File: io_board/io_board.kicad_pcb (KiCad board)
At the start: 2 copper layers, 70 x 100 mm, 54 parts, among them J1 RATE_CV1, J10 CLK_2, J11 SAW_2, J12 MIX, J13 IN2, J14 OUT2, J16 Conn_01x10_Male, J2 PWM_1, J3 CLK_1, J4 SAW_1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

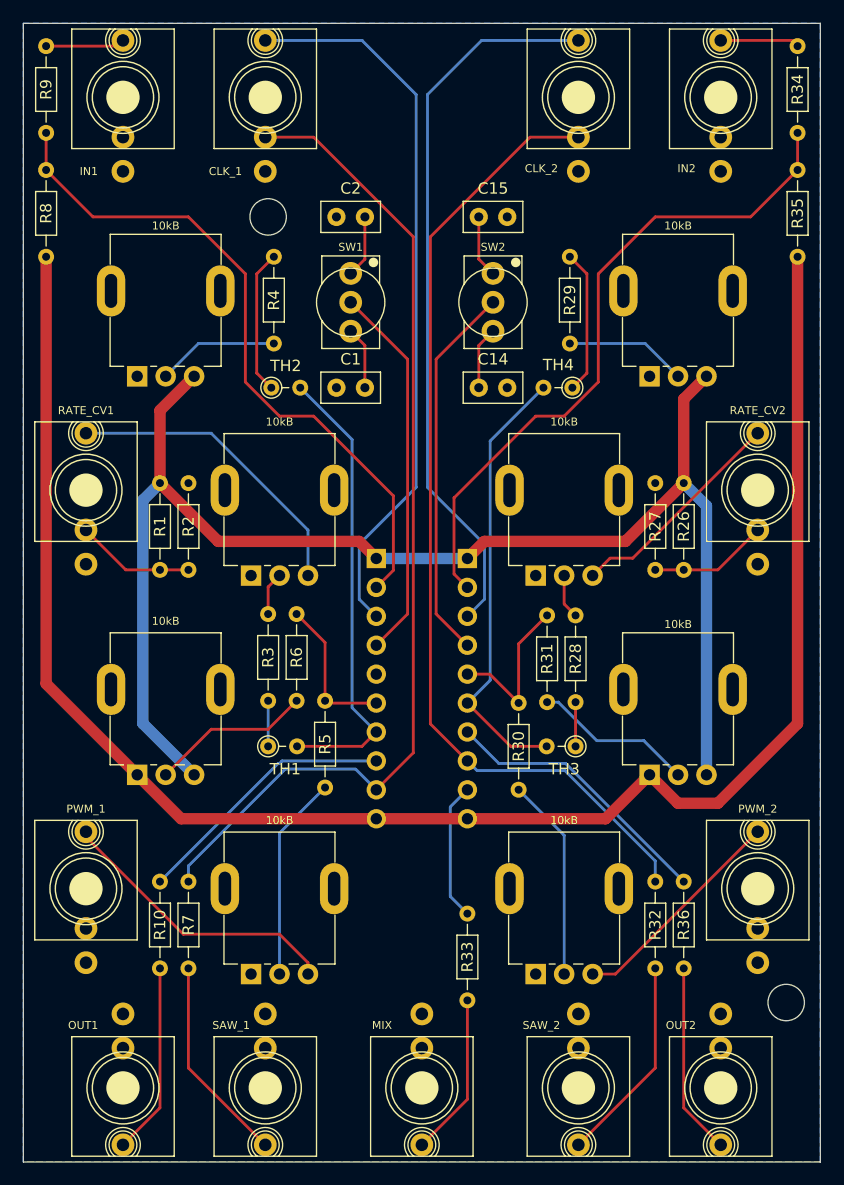
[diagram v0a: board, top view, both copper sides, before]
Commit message: Changed mounting holes
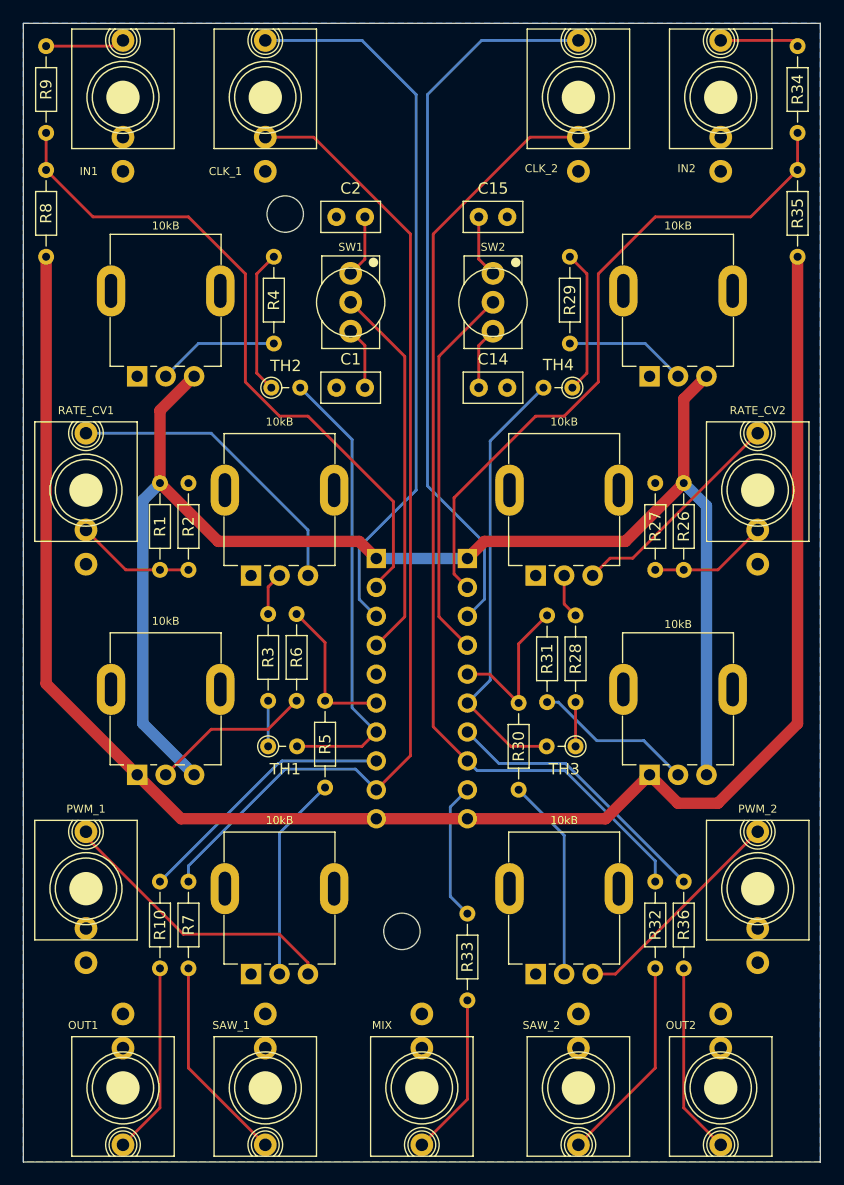
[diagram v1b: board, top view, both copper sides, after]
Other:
- outline, holes or cut-outs redrawn
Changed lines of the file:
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@@
     )
   )
+  (gr_circle (center 23 16.75) (end 24.6 16.75) (layer "Edge.Cuts") (width 0.1) (fill none))
   (gr_rect (start 0 100) (end 70 0) (layer "Edge.Cuts") (width 0.1) (fill none))
-  (gr_circle (center 67 86) (end 68.6 86) (layer "Edge.Cuts") (width 0.1) (fill none))
-  (gr_circle (center 21.5 17) (end 23.1 17) (layer "Edge.Cuts") (width 0.1) (fill none))
+  (gr_circle (center 33.25 79.75) (end 34.85 79.75) (layer "Edge.Cuts") (width 0.1) (fill none))
   (gr_circle (center 57.5 23.5) (end 61.1 23.5) (layer "User.2") (width 0.15) (fill none))
   (gr_circle (center 12.5 58.5) (end 16.1 58.5) (layer "User.2") (width 0.15) (fill none))
@@
   (gr_circle (center 48.75 93.5) (end 51.95 93.5) (layer "User.2") (width 0.15) (fill none))
   (gr_circle (center 22.5 41) (end 26.1 41) (layer "User.2") (width 0.15) (fill none))
-  (gr_line (start 70 50) (end 0 50) (layer "User.2") (width 0.15))
+  (gr_line (start 70.5 50) (end 0.5 50) (layer "User.2") (width 0.15))
   (gr_circle (center 5.5 41) (end 8.7 41) (layer "User.2") (width 0.15) (fill none))
   (gr_circle (center 35 93.5) (end 38.2 93.5) (layer "User.2") (width 0.15) (fill none))
@@
   (segment (start 5.5 71) (end 5.5 71.45) (width 0.25) (layer "F.Cu") (net 8))
   (segment (start 5.5 71.45) (end 14.05 80) (width 0.25) (layer "F.Cu") (net 8))
+  (segment (start 31 52.08) (end 29.5 50.58) (width 0.25) (layer "B.Cu") (net 9))
+  (segment (start 34.5 41) (end 34.5 6.25) (width 0.25) (layer "B.Cu") (net 9))
+  (segment (start 29.5 50.58) (end 29.5 46) (width 0.25) (layer "B.Cu") (net 9))
+  (segment (start 29.5 46) (end 34.5 41) (width 0.25) (layer "B.Cu") (net 9))
+  (segment (start 34.5 6.25) (end 29.75 1.5) (width 0.25) (layer "B.Cu") (net 9))
   (segment (start 29.75 1.5) (end 21.25 1.5) (width 0.25) (layer "B.Cu") (net 9))
-  (segment (start 34.5 6.25) (end 29.75 1.5) (width 0.25) (layer "B.Cu") (net 9))
-  (segment (start 29.5 50.58) (end 29.5 45.75) (width 0.25) (layer "B.Cu") (net 9))
-  (segment (start 29.5 45.75) (end 34.5 40.75) (width 0.25) (layer "B.Cu") (net 9))
-  (segment (start 31 52.08) (end 29.5 50.58) (width 0.25) (layer "B.Cu") (net 9))
-  (segment (start 34.5 40.75) (end 34.5 6.25) (width 0.25) (layer "B.Cu") (net 9))
-  (segment (start 34.25 18.75) (end 25.5 10) (width 0.25) (layer "F.Cu") (net 10))
+  (segment (start 34 64.32) (end 34 18.5) (width 0.25) (layer "F.Cu") (net 10))
   (segment (start 25.5 10) (end 21.25 10) (width 0.25) (layer "F.Cu") (net 10))
-  (segment (start 31 67.32) (end 34.25 64.07) (width 0.25) (layer "F.Cu") (net 10))
-  (segment (start 34.25 64.07) (end 34.25 18.75) (width 0.25) (layer "F.Cu") (net 10))
+  (segment (start 31 67.32) (end 34 64.32) (width 0.25) (layer "F.Cu") (net 10))
+  (segment (start 34 18.5) (end 25.5 10) (width 0.25) (layer "F.Cu") (net 10))
   (segment (start 29.18 65.5) (end 31 67.32) (width 0.25) (layer "B.Cu") (net 10))
   (segment (start 14.5 75.38) (end 14.5 74) (width 0.25) (layer "B.Cu") (net 10))
@@
   (segment (start 52 83.5) (end 64.5 71) (width 0.25) (layer "F.Cu") (net 16))
   (segment (start 50 83.5) (end 52 83.5) (width 0.25) (layer "F.Cu") (net 16))
-  (segment (start 35.5 40.75) (end 35.5 6.25) (width 0.25) (layer "B.Cu") (net 17))
+  (segment (start 35.5 6.25) (end 40.25 1.5) (width 0.25) (layer "B.Cu") (net 17))
   (segment (start 39 52.08) (end 40.5 50.58) (width 0.25) (layer "B.Cu") (net 17))
-  (segment (start 35.5 6.25) (end 40.25 1.5) (width 0.25) (layer "B.Cu") (net 17))
-  (segment (start 40.5 50.58) (end 40.5 45.75) (width 0.25) (layer "B.Cu") (net 17))
+  (segment (start 40.5 50.58) (end 40.5 45.625) (width 0.25) (layer "B.Cu") (net 17))
+  (segment (start 35.5 40.625) (end 35.5 6.25) (width 0.25) (layer "B.Cu") (net 17))
+  (segment (start 40.5 45.625) (end 35.5 40.625) (width 0.25) (layer "B.Cu") (net 17))
   (segment (start 40.25 1.5) (end 48.75 1.5) (width 0.25) (layer "B.Cu") (net 17))
-  (segment (start 40.5 45.75) (end 35.5 40.75) (width 0.25) (layer "B.Cu") (net 17))
-  (segment (start 39 64.78) (end 35.75 61.53) (width 0.25) (layer "F.Cu") (net 18))
   (segment (start 44.5 10) (end 48.75 10) (width 0.25) (layer "F.Cu") (net 18))
-  (segment (start 35.75 61.53) (end 35.75 18.75) (width 0.25) (layer "F.Cu") (net 18))
-  (segment (start 35.75 18.75) (end 44.5 10) (width 0.25) (layer "F.Cu") (net 18))
+  (segment (start 36 61.78) (end 36 18.5) (width 0.25) (layer "F.Cu") (net 18))
+  (segment (start 36 18.5) (end 44.5 10) (width 0.25) (layer "F.Cu") (net 18))
+  (segment (start 39 64.78) (end 36 61.78) (width 0.25) (layer "F.Cu") (net 18))
   (segment (start 39 64.78) (end 39.85 65.63) (width 0.25) (layer "B.Cu") (net 18))
   (segment (start 55.5 73.567845) (end 55.5 75.38) (width 0.25) (layer "B.Cu") (net 18))
@@
   (segment (start 12 40.38) (end 10.5 41.88) (width 1) (layer "B.Cu") (net 23))
   (segment (start 10.5 61.5) (end 15 66) (width 1) (layer "B.Cu") (net 23))
+  (segment (start 25 34.5) (end 22.5 34.5) (width 0.25) (layer "F.Cu") (net 24))
+  (segment (start 32.5 47.725499) (end 32.5 42) (width 0.25) (layer "F.Cu") (net 24))
+  (segment (start 32.5 42) (end 25 34.5) (width 0.25) (layer "F.Cu") (net 24))
+  (segment (start 19.5 22) (end 14.5 17) (width 0.25) (layer "F.Cu") (net 24))
   (segment (start 22.5 34.5) (end 19.5 31.5) (width 0.25) (layer "F.Cu") (net 24))
+  (segment (start 2 12.88) (end 2 9.62) (width 0.25) (layer "F.Cu") (net 24))
+  (segment (start 6.12 17) (end 2 12.88) (width 0.25) (layer "F.Cu") (net 24))
   (segment (start 14.5 17) (end 6.12 17) (width 0.25) (layer "F.Cu") (net 24))
-  (segment (start 32.5 48.04) (end 32.5 41.5) (width 0.25) (layer "F.Cu") (net 24))
-  (segment (start 25.5 34.5) (end 22.5 34.5) (width 0.25) (layer "F.Cu") (net 24))
+  (segment (start 31 49.54) (end 31 49.225499) (width 0.25) (layer "F.Cu") (net 24))
+  (segment (start 31 49.225499) (end 32.5 47.725499) (width 0.25) (layer "F.Cu") (net 24))
   (segment (start 19.5 31.5) (end 19.5 22) (width 0.25) (layer "F.Cu") (net 24))
-  (segment (start 19.5 22) (end 14.5 17) (width 0.25) (layer "F.Cu") (net 24))
-  (segment (start 6.12 17) (end 2 12.88) (width 0.25) (layer "F.Cu") (net 24))
-  (segment (start 2 12.88) (end 2 9.62) (width 0.25) (layer "F.Cu") (net 24))
-  (segment (start 31 49.54) (end 32.5 48.04) (width 0.25) (layer "F.Cu") (net 24))
-  (segment (start 32.5 41.5) (end 25.5 34.5) (width 0.25) (layer "F.Cu") (net 24))
   (segment (start 29.74 63.5) (end 31 62.24) (width 0.25) (layer "F.Cu") (net 25))
   (segment (start 24.04 63.5) (end 29.74 63.5) (width 0.25) (layer "F.Cu") (net 25))
@@
   (segment (start 31 59.7) (end 26.7 59.7) (width 0.25) (layer "F.Cu") (net 26))
   (segment (start 26.7 59.7) (end 26.5 59.5) (width 0.25) (layer "F.Cu") (net 26))
-  (segment (start 33.75 29.5) (end 28.75 24.5) (width 0.25) (layer "F.Cu") (net 27))
-  (segment (start 31 54.62) (end 33.75 51.87) (width 0.25) (layer "F.Cu") (net 27))
-  (segment (start 33.75 51.87) (end 33.75 29.5) (width 0.25) (layer "F.Cu") (net 27))
+  (segment (start 31 54.62) (end 33.5 52.12) (width 0.25) (layer "F.Cu") (net 27))
+  (segment (start 33.5 29.25) (end 28.75 24.5) (width 0.25) (layer "F.Cu") (net 27))
+  (segment (start 33.5 52.12) (end 33.5 29.25) (width 0.25) (layer "F.Cu") (net 27))
   (segment (start 22.38 65) (end 12 75.38) (width 0.25) (layer "B.Cu") (net 28))
   (segment (start 31 64.78) (end 22.72 64.78) (width 0.25) (layer "B.Cu") (net 28))
@@
   (segment (start 43.5 59.69) (end 43.5 54.5) (width 0.25) (layer "F.Cu") (net 32))
   (segment (start 39 57.16) (end 40.97 57.16) (width 0.25) (layer "F.Cu") (net 32))
-  (segment (start 36.25 51.87) (end 39 54.62) (width 0.25) (layer "F.Cu") (net 33))
-  (segment (start 41.25 24.5) (end 36.25 29.5) (width 0.25) (layer "F.Cu") (net 33))
-  (segment (start 36.25 29.5) (end 36.25 51.87) (width 0.25) (layer "F.Cu") (net 33))
+  (segment (start 36.5 52.12) (end 39 54.62) (width 0.25) (layer "F.Cu") (net 33))
+  (segment (start 36.5 29.25) (end 36.5 52.12) (width 0.25) (layer "F.Cu") (net 33))
+  (segment (start 41.25 24.5) (end 36.5 29.25) (width 0.25) (layer "F.Cu") (net 33))
   (segment (start 37.5 76.69) (end 37.5 68.82) (width 0.25) (layer "B.Cu") (net 34))
   (segment (start 39 78.19) (end 37.5 76.69) (width 0.25) (layer "B.Cu") (net 34))
